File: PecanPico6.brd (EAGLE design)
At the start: 50 x 29.8 mm, 79 parts, among them IC1 TPS79718DCKT, IC2 SI4463/4, IC3 UBLOX_MAX-6, IC4 LPC1114FHN33/333, IC5 SPV1040, IC6 AS213-92LF, IC7 BMP180, Q2 AP2301

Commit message: Initial commit of new PecanPico6b degin
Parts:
- removed JP5: (no value), pinhead:2X06
- removed LED2: red, SparkFun:LED-0603
- removed LED3: blue, SparkFun:LED-0603
- removed R13, R5: 1k, sven:0402
- removed R17: 22k, sven:0402
- removed R18: 10k, sven:0402
- removed SJ1, SJ2, SJ3, SJ4, SJ5: (no value), jumper:SJ
- removed SJ7: (no value), jumper:SJ_2
- removed TP1, TP2: TPTP07R, testpad:TP07R
- added C8: 100nF, sven:0402
- added JP1, JP6, JP7: (no value), pinhead:2X04
- moved C2 30.7 mm to (35.0, 36.2)
- moved C22 20.0 mm to (16.7, 16.8), turned to 90 degrees
- moved C13 18.9 mm to (5.60, 16.1), turned to 0 degrees
- moved C14 17.7 mm to (11.0, 19.8), turned to 90 degrees
- moved UART 17.3 mm to (39.8, 0.80), turned to 270 degrees
- moved IC7 16.7 mm to (20.6, 10.8), turned to 0 degrees
- moved R2 16.0 mm to (12.1, 19.8), turned to 90 degrees
- moved R1 14.4 mm to (13.2, 19.8), turned to 270 degrees
- moved C21 14.4 mm to (31.9, 26.9)
- moved JP3 13.6 mm to (5.80, 22.1)
- moved C19 13.3 mm to (33.0, 28.3)
- moved R11 13.3 mm to (33.0, 29.3)
- moved R12 13.3 mm to (33.0, 27.3)
- moved R16 13.3 mm to (33.0, 30.3)
- moved C18 13.3 mm to (34.3, 28.3)
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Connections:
- removed net ADC_VSOL: IC4.22, R17.P$1, R18.P$2
- removed net LDO_EN: IC1.1, IC4.24
- removed net N$15: IC3.3_RXD1, SJ1.1
- removed net N$2: C24.P$1, SJ7.2
- removed net N$20: IC3.2_TXD1, SJ2.1
- removed net N$25: IC3.16_SDA2, SJ3.2
- removed net N$26: IC3.17_SCL2, SJ4.2
- removed net N$4: C22.P$2, IC4.4
- removed net N$6: LED2.C, R5.P$2
- removed net N$8: IC3.4_TIMEPULSE, R5.P$1
- removed net N$9: LED3.C, R13.P$2
- new net TIMEPULSE: IC3.4_TIMEPULSE, IC4.27
- net GND: now also C8.P$1, JP1.6, JP1.7; no longer JP5.10, JP5.11, JP5.12, JP5.3, R13.P$1, R18.P$1, TP2.TP
- net I2C_PULL_VCC: now also IC4.9; no longer IC4.12
- net ISP_ENTRY: no longer TP1.TP
- net N$10: now also C24.P$1; no longer SJ7.3
- net N$13: now also C22.P$2; no longer C22.P$1
- net N$17: now also C22.P$1; no longer SJ7.1
- net N$5: now also C8.P$2; no longer SJ5.1
- net OUT1: no longer JP5.8
- net OUT2: now also IC4.24; no longer IC4.27, JP5.6
- net OUT3: no longer JP5.4
- net OUT4: no longer JP5.2
- net RESET: now also JP1.1; no longer JP5.5
- net RXD: no longer SJ2.2
- net SCL: now also IC3.17_SCL2, JP1.4; no longer SJ4.1
- net SDA: now also IC3.16_SDA2, JP1.2; no longer SJ3.1
- net SWCLK: now also JP1.5; no longer JP5.9
- net SWDIO: now also JP1.3; no longer JP5.7
- net TXD: no longer SJ1.2
- net TX_EN: no longer LED3.A
- net VCC15: now also IC1.1, JP1.8; no longer JP5.1, LED2.A, SJ5.2
- net VCXO_EN: now also IC4.12; no longer IC4.9
- net VSOLAR: now also IC4.22; no longer R17.P$2
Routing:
- net VCC15: track 122.6 -> 27.9 mm, vias 16 -> 2
- net SDA: track 38.1 -> 0.00 mm, vias 2 -> 0
- net GND: track 37.6 -> 0.00 mm, vias 54 -> 10
- net SCL: track 36.8 -> 0.00 mm, vias 2 -> 0
- net N$13: track 32.3 -> 3.84 mm, vias 4 -> 0
- net IRQ: track 27.0 -> 0.00 mm, vias 2 -> 0
- net SWCLK: track 26.7 -> 0.00 mm, vias 4 -> 0
- net LDO_EN: track 25.0 -> 0.00 mm, vias 2 -> 0
- net MOSI: track 22.0 -> 0.00 mm, vias 2 -> 0
- net RADIO_SDN: track 21.8 -> 0.00 mm, vias 2 -> 0
- net SS: track 21.7 -> 0.00 mm, vias 2 -> 0
- net MISO: track 21.4 -> 0.00 mm, vias 2 -> 0
- net SCK: track 20.9 -> 0.00 mm, vias 2 -> 0
- net GPS_RESET: track 20.4 -> 0.00 mm, vias 3 -> 0
- net GPIO0: track 20.0 -> 0.00 mm, vias 2 -> 0
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- removed copper zone on layer 1, net GND
- removed copper zone on layer 16, net GND
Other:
- board text added: "Version 11. July 2015"
- board text removed: "Version 03. April 2015"

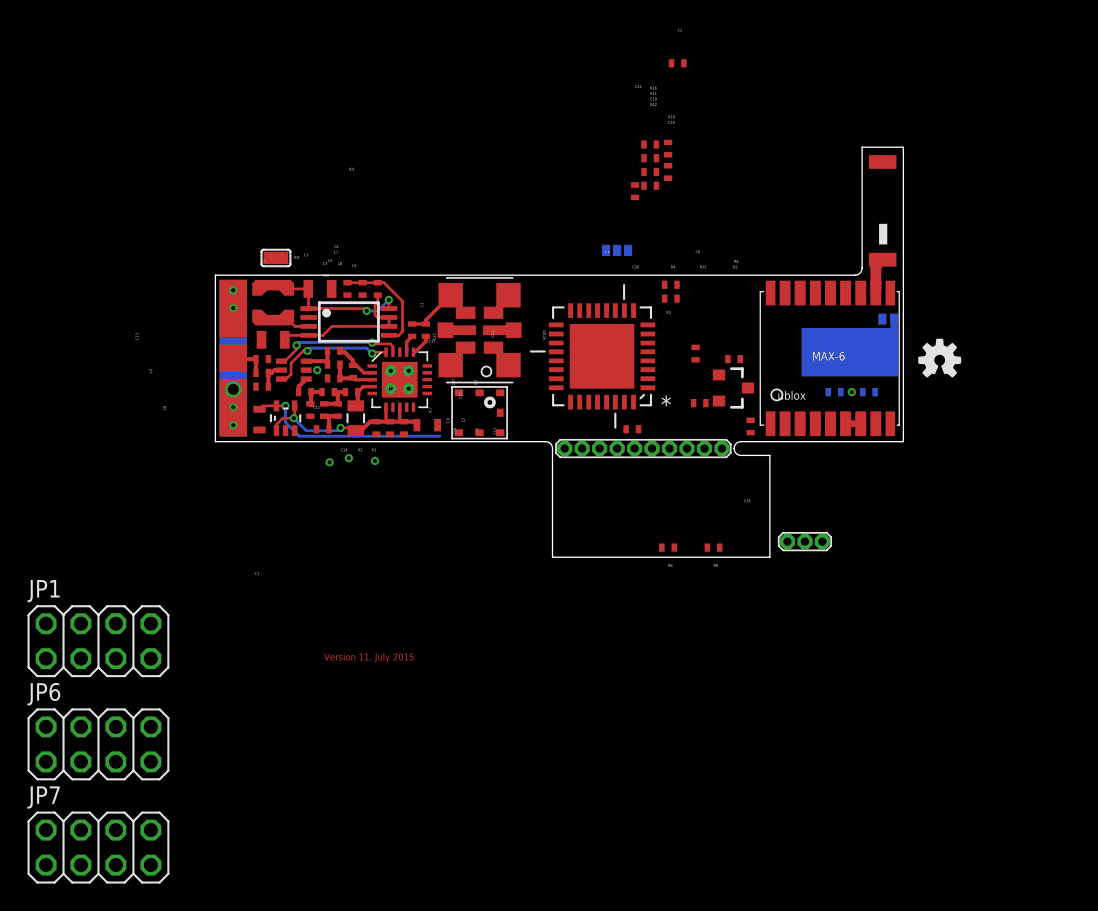
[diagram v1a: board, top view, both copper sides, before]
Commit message: Moved microcontroller
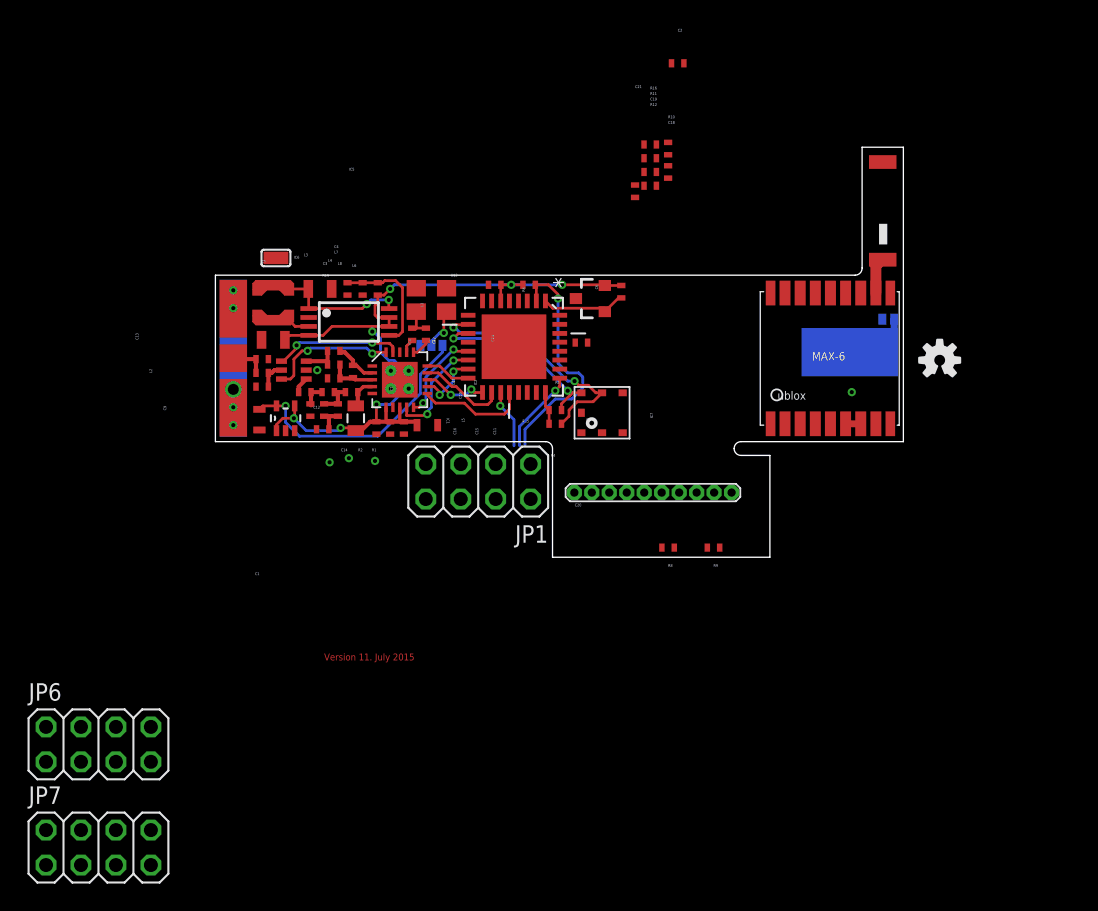
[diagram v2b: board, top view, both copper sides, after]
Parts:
- removed C25, C8: 100nF, sven:0402
- removed R7: 10k, sven:0402
- removed UART: PINHEAD_PINHD-1X10S, 1_27x3:PINHEAD_1X10S
- removed VCXO: OSCILLATORSMD6, SparkFun-FreqCtrl_TK:CRYSTAL-SMD-7.5X5.2-6PIN
- added U$2: VCXO, sven:VCXO_3.2X2.5MM
- moved JP1 29.9 mm to (20.5, 5.80), turned to 180 degrees
- moved C6 15.4 mm to (21.7, 20.1), turned to 0 degrees
- moved SJ8 15.2 mm to (17.1, 15.7), turned to 180 degrees
- moved R15 15.1 mm to (24.2, 20.1), turned to 180 degrees
- moved R3 12.4 mm to (26.1, 11.0), turned to 180 degrees
- moved R4 12.4 mm to (26.1, 10.0), turned to 180 degrees
- moved Q2 12.2 mm to (28.7, 19.1), turned to 90 degrees
- moved R6 9.55 mm to (30.9, 19.6), turned to 270 degrees
- moved IC7 8.90 mm to (29.5, 10.8), turned to 180 degrees
- moved C20 7.31 mm to (28.0, 15.9), turned to 180 degrees
- moved IC4 6.44 mm to (23.1, 15.6), turned to 270 degrees
- moved JP2 3.28 mm to (33.2, 5.00)
- moved C22 0.30 mm to (16.7, 16.5)
- moved C24 0.30 mm to (15.7, 16.5)
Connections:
- removed net ISP_ENTRY: IC4.3
- removed net OUT1: IC4.26, JP2.3
- removed net OUT2: IC4.24, JP2.4
- removed net OUT3: IC4.28, JP2.5
- removed net OUT4: IC4.30, JP2.6
- net GND: now also U$2.P$2; no longer C25.P$1, C8.P$1, UART.P$3, VCXO.3, VCXO.3INNER
- net GPIO0: now also IC4.14; no longer IC4.13
- net GPIO1: now also IC4.13; no longer IC4.14
- net GPS_OFF: now also IC4.1; no longer IC4.7
- net GPS_RESET: now also IC4.7; no longer IC4.1, R7.P$1
- net I2C_PULL_VCC: now also IC4.24; no longer IC4.9
- net IRQ: now also IC4.20; no longer IC4.8
- net N$13: now also U$2.P$3; no longer VCXO.4, VCXO.4INNER
- net N$14: now also U$2.P$4; no longer VCXO.6, VCXO.6INNER
- net N$21: now also U$2.P$1; no longer VCXO.1, VCXO.1INNER
- net N$5: no longer C25.P$2, C8.P$2
- net RADIO_SDN: no longer IC4.20
- net RXD: no longer UART.P$2
- net TXD: no longer UART.P$1
- net VCC15: no longer R7.P$2, SJ8.1
- net VCXO_EN: now also SJ8.1; no longer IC4.12, VCXO.2, VCXO.2INNER
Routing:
- net VCC15: track 27.9 -> 58.1 mm, vias 2 -> 7
- net SCL: track 0.00 -> 18.1 mm, vias 0 -> 2
- net RESET: track 0.00 -> 17.8 mm, vias 0 -> 1
- net SDA: track 0.00 -> 13.7 mm, vias 0 -> 2
- net IRQ: track 0.00 -> 8.01 mm
- net GPIO0: track 0.00 -> 7.92 mm, vias 0 -> 2
- net GPIO1: track 0.00 -> 6.76 mm, vias 0 -> 2
- net GPS_OFF: track 0.00 -> 6.40 mm
- net MOSI: track 0.00 -> 6.34 mm
- net SWDIO: track 0.00 -> 6.13 mm, vias 0 -> 1
- net MISO: track 0.00 -> 4.73 mm, vias 0 -> 2
- net SCK: track 0.00 -> 4.52 mm, vias 0 -> 2
- net SWCLK: track 0.00 -> 4.30 mm, vias 0 -> 1
- net VCC1V8: track 14.8 -> 18.9 mm
- net SS: track 0.00 -> 3.34 mm
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
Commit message: Sorted parts
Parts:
- removed IC3: UBLOX_MAX-6, ava:UBLOX_MAX-6
- removed U$3: JTI_ANTENNA-1575AT43A40, ava:JTI_ANTENNA-1575AT43A40
- added U$4: UBLOX_CAM, ava:UBLOX_CAM-M8
- moved C2 38.1 mm to (6.30, 11.1), flipped to the bottom
- moved R8 35.4 mm to (18.4, 32.6)
- moved R9 34.9 mm to (22.5, 32.5)
- moved IC7 23.7 mm to (5.80, 11.0), turned to 270 degrees
- moved JP1 22.0 mm to (21.8, 27.8), turned to 0 degrees
- moved C1 22.0 mm to (24.4, 19.8), turned to 180 degrees
- moved IC1 21.8 mm to (26.3, 19.5), turned to 0 degrees
- moved JP2 20.5 mm to (21.7, 22.0)
- moved C21 17.7 mm to (17.6, 16.5)
- moved C18 16.8 mm to (20.7, 18.5), turned to 0 degrees
- moved R10 16.5 mm to (22.4, 18.5), turned to 0 degrees
- moved R12 15.3 mm to (19.7, 19.8), turned to 90 degrees
- moved C19 15.0 mm to (20.7, 19.8), turned to 90 degrees
- moved R11 14.8 mm to (21.7, 19.8), turned to 270 degrees
- moved R16 14.7 mm to (22.7, 19.8), turned to 270 degrees
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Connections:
- removed net N$3: IC3.11_RF_IN, U$3.FEED
- new net N$2: U$4.16/ANT, U$4.17/RF_IN
- net GND: now also U$4.10/GND, U$4.11/GND, U$4.12/GND, U$4.13/GND, U$4.14/GND, U$4.15/GND, U$4.18/GND, U$4.19/GND, U$4.21/GND, U$4.22/GND, U$4.27/GND, U$4.31/GND, U$4.4/GND, U$4.5/GND; no longer IC3.10_GND, IC3.12_GND, IC3.1_GND, JP1.6
- net GPIO0: now also IC4.32; no longer IC4.14
- net GPIO1: now also IC4.31; no longer IC4.13
- net GPS_OFF: now also IC4.26; no longer IC4.1
- net GPS_RESET: now also IC4.8, U$4.23/RESET_N; no longer IC3.9_V_RESET, IC4.7
- net I2C_PULL_VCC: now also IC4.9; no longer IC4.24
- net IRQ: now also IC4.30; no longer IC4.20
- net N$5: now also U$4.9/VCC; no longer IC3.8_VCC
- net RXD: now also IC4.13; no longer IC4.31
- net SCL: now also U$4.6/SCL; no longer IC3.17_SCL2, JP1.4
- net SDA: now also U$4.3/SDA; no longer IC3.16_SDA2, JP1.2
- net SS: now also IC4.1; no longer IC4.16
- net TIMEPULSE: now also IC4.16, U$4.29/TIMEPULSE; no longer IC3.4_TIMEPULSE, IC4.27
- net TXD: now also IC4.14; no longer IC4.32
- net VCC15: now also U$4.1/VCC_IO, U$4.8/V_BCKP; no longer IC3.6_V_BCKP, IC3.7_VCC_IO, JP1.8
- net VCC1V8: now also IC4.20
- net VSOLAR: now also IC4.24; no longer IC4.22
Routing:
- net SDA: track 13.7 -> 27.2 mm
- net VCC1V8: track 18.9 -> 8.28 mm
- net VSOLAR: track 13.7 -> 24.1 mm, vias 2 -> 4
- net MOSI: track 6.34 -> 16.5 mm, vias 0 -> 2
- net SCL: track 18.1 -> 27.7 mm
- net SCK: track 4.52 -> 13.2 mm
- net VCC15: track 58.1 -> 66.4 mm, vias 7 -> 5
- net MISO: track 4.73 -> 12.6 mm
- net GPS_OFF: track 6.40 -> 0.00 mm
- net N$21: track 0.00 -> 4.90 mm
- net IRQ: track 8.01 -> 3.52 mm
- net SS: track 3.34 -> 7.40 mm, vias 0 -> 2
- net SWDIO: track 6.13 -> 2.88 mm
- net MOD1: track 0.00 -> 3.20 mm
- net I2C_PULL_VCC: track 2.38 -> 5.32 mm
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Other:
- board size 50 x 29.8 mm -> 50 x 12.1 mm

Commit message: Done some more sorting
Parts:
- removed C17: 2.2uF, sven:0603
- removed JP2: (no value), PecanPico5a:1_27X3_PINHEAD_1X10S
- removed U$4: UBLOX_CAM, ava:UBLOX_CAM-M8
- added C8: 2.2uF, sven:0402
- added U$3: UBLOX_CAM, Ava:UBLOX_CAM-M8
- C1: device sven:0603 -> sven:0402
- moved JP1 41.1 mm to (60.9, 15.0), turned to 90 degrees
- moved R8 40.3 mm to (56.2, 18.7)
- moved R9 39.8 mm to (56.0, 11.1)
- moved SJ6 17.9 mm to (34.6, 26.2)
- moved C1 13.1 mm to (16.1, 9.70), turned to 270 degrees
- moved R6 10.8 mm to (35.0, 23.5)
- moved Q2 10.6 mm to (30.8, 23.4)
- moved JP4 10.4 mm to (41.6, 23.8)
- moved SJ8 2.28 mm to (17.0, 17.1)
- moved R15 1.70 mm to (18.0, 9.70), turned to 270 degrees
- moved JP3 0.87 mm to (4.65, 19.4), turned to 90 degrees
- moved C20 0.72 mm to (18.2, 14.8), turned to 0 degrees
- moved C18 0.71 mm to (20.0, 18.4)
- moved R10 0.71 mm to (21.7, 18.4)
- moved C13 0.20 mm to (5.40, 17.0)
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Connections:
- net GND: now also C1.P$2, C8.P$1, U$3.10/GND, U$3.11/GND, U$3.12/GND, U$3.13/GND, U$3.14/GND, U$3.15/GND, U$3.18/GND, U$3.19/GND, U$3.21/GND, U$3.22/GND, U$3.27/GND, U$3.31/GND, U$3.4/GND, U$3.5/GND; no longer C1.P$1, C17.P$2, JP2.10, U$4.10/GND, U$4.11/GND, U$4.12/GND, U$4.13/GND, U$4.14/GND, U$4.15/GND, U$4.18/GND, U$4.19/GND, U$4.21/GND, U$4.22/GND, U$4.27/GND, U$4.31/GND, U$4.4/GND, U$4.5/GND
- net GPIO0: no longer IC4.32
- net GPIO1: now also IC4.32; no longer IC4.31
- net GPS_RESET: now also U$3.23/RESET_N; no longer U$4.23/RESET_N
- net IRQ: now also IC4.31; no longer IC4.30
- net N$2: now also U$3.16/ANT, U$3.17/RF_IN; no longer U$4.16/ANT, U$4.17/RF_IN
- net N$5: now also U$3.9/VCC; no longer U$4.9/VCC
- net RESET: no longer JP2.8
- net RXD: now also JP1.4
- net SCL: now also U$3.6/SCL; no longer U$4.6/SCL
- net SDA: now also U$3.3/SDA; no longer U$4.3/SDA
- net SS: now also IC4.30; no longer IC4.1
- net SWCLK: no longer JP2.1
- net SWDIO: no longer JP2.2
- net TIMEPULSE: now also U$3.29/TIMEPULSE; no longer U$4.29/TIMEPULSE
- net TXD: now also JP1.2
- net VCC15: now also C1.P$1, U$3.1/VCC_IO, U$3.8/V_BCKP; no longer C17.P$1, JP2.9, U$4.1/VCC_IO, U$4.8/V_BCKP
- net VCC1V8: now also C8.P$2; no longer C1.P$2, IC4.23
- net VCXO_CTRL: now also IC4.23; no longer IC4.21
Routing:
- net SWDIO: track 2.88 -> 15.8 mm
- net VCXO_EN: track 0.00 -> 8.75 mm, vias 0 -> 1
- net TIMEPULSE: track 0.00 -> 7.22 mm
- net TXD: track 0.00 -> 6.84 mm
- net RXD: track 0.00 -> 6.80 mm
- net SWCLK: track 3.57 -> 10.2 mm, vias 0 -> 1
- net GPS_RESET: track 1.23 -> 7.80 mm, vias 1 -> 0
- net GPIO0: track 5.73 -> 0.00 mm
- net N$7: track 5.63 -> 0.00 mm
- net MISO: track 12.6 -> 17.7 mm
- net VCC15: track 66.4 -> 70.0 mm
- net SS: track 7.40 -> 4.01 mm, vias 2 -> 0
- net VCC1V8: track 8.28 -> 10.9 mm
- net VSOLAR: track 24.1 -> 26.6 mm
- net N$14: track 3.42 -> 4.80 mm
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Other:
- board size 50 x 12.1 mm -> 50 x 12 mm

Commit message: Moved stuff around the PCB
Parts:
- moved JP1 19.4 mm to (41.5, 15.0)
- moved R6 15.6 mm to (27.8, 9.70), turned to 90 degrees
- moved U$3 13.3 mm to (37.9, 15.2), flipped to the bottom, turned to 180 degrees
- moved Q2 12.9 mm to (30.0, 10.5), turned to 270 degrees
- moved R9 11.7 mm to (45.3, 15.8), turned to 90 degrees
- moved R8 10.9 mm to (45.3, 18.4), turned to 90 degrees
- moved C6 6.04 mm to (18.7, 10.0), turned to 270 degrees
- moved R4 3.50 mm to (30.3, 14.0), turned to 90 degrees
- moved IC1 2.10 mm to (28.4, 19.4)
- moved C8 2.00 mm to (25.7, 19.8), turned to 0 degrees
- moved R3 1.17 mm to (29.3, 14.0), turned to 90 degrees
- moved R15 0.42 mm to (17.7, 10.0)
- moved R16 0.42 mm to (23.0, 20.0), turned to 0 degrees
- moved C20 0.20 mm to (18.0, 14.8)
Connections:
- net GND: now also JP1.6
- net GPS_OFF: now also IC4.9; no longer IC4.26
- net I2C_PULL_VCC: now also IC4.12; no longer IC4.9
- net RXD: no longer JP1.4
- net SCL: now also JP1.4
- net SDA: now also JP1.2
- net TXD: no longer JP1.2
- net VCC15: now also JP1.8
- net VSOLAR: now also IC4.27; no longer IC4.24
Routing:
- net SDA: track 27.2 -> 51.8 mm, vias 2 -> 4
- net SCL: track 27.7 -> 50.6 mm, vias 2 -> 3
- net VCC15: track 70.0 -> 80.8 mm, vias 5 -> 7
- net N$5: track 0.00 -> 9.71 mm, vias 0 -> 1
- net RXD: track 6.80 -> 14.2 mm
- net TXD: track 6.84 -> 14.2 mm
- net SWCLK: track 10.2 -> 17.0 mm, vias 1 -> 0
- net SWDIO: track 15.8 -> 21.9 mm, vias 1 -> 2
- net GPS_RESET: track 7.80 -> 2.48 mm, vias 0 -> 1
- net RESET: track 20.0 -> 25.0 mm, vias 1 -> 2
- net GPS_OFF: track 0.00 -> 4.27 mm
- net MISO: track 17.7 -> 20.5 mm
- net MOSI: track 17.2 -> 14.7 mm
- net VCC1V8: track 10.9 -> 13.4 mm
- net TIMEPULSE: track 7.22 -> 4.93 mm, vias 0 -> 1
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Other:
- board size 50 x 12 mm -> 44.7 x 12.1 mm
- board text added: "Version 14. July 2015"
- board text removed: "Version 11. July 2015"
